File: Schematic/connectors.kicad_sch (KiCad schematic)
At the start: 32 parts, among them J10 PIN2216, J11 PIN2216, J12 PIN2216, J2 PIN2216, J3 PIN2216, J4 PIN2216, J5 PIN2216, J6 PIN2216, J7 PIN2216, J8 PIN2216, J9 PIN2216, U10 HDGC1002WR-S-4P, U11 HDGC1002WR-S-4P, U14 HDGC1002WR-S-4P, U15 HDGC1002WR-S-6P, U16 HDGC1002WR-S-8P, U17 HDGC1002WR-S-8P, U7 HDGC1002WR-S-4P, U8 HDGC1002WR-S-4P, U9 HDGC1002WR-S-4P

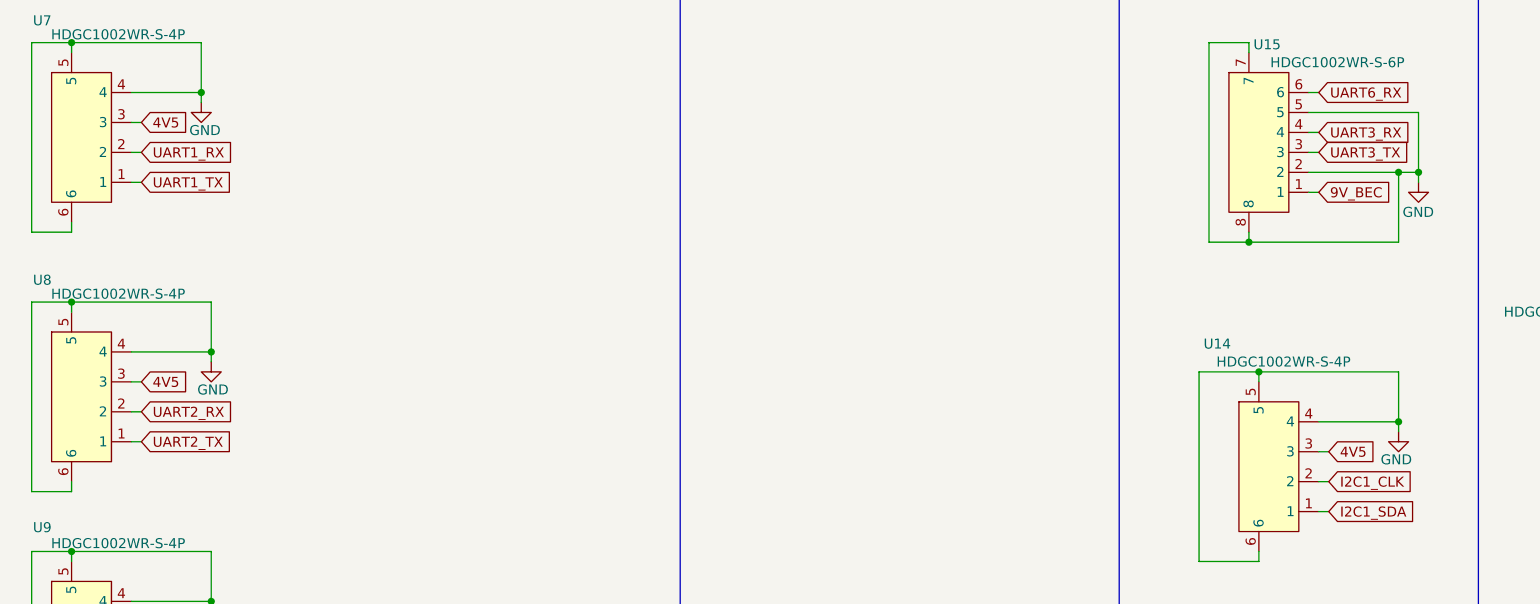
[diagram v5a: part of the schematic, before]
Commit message: Added power zones in Inner2.cu layer for better power management
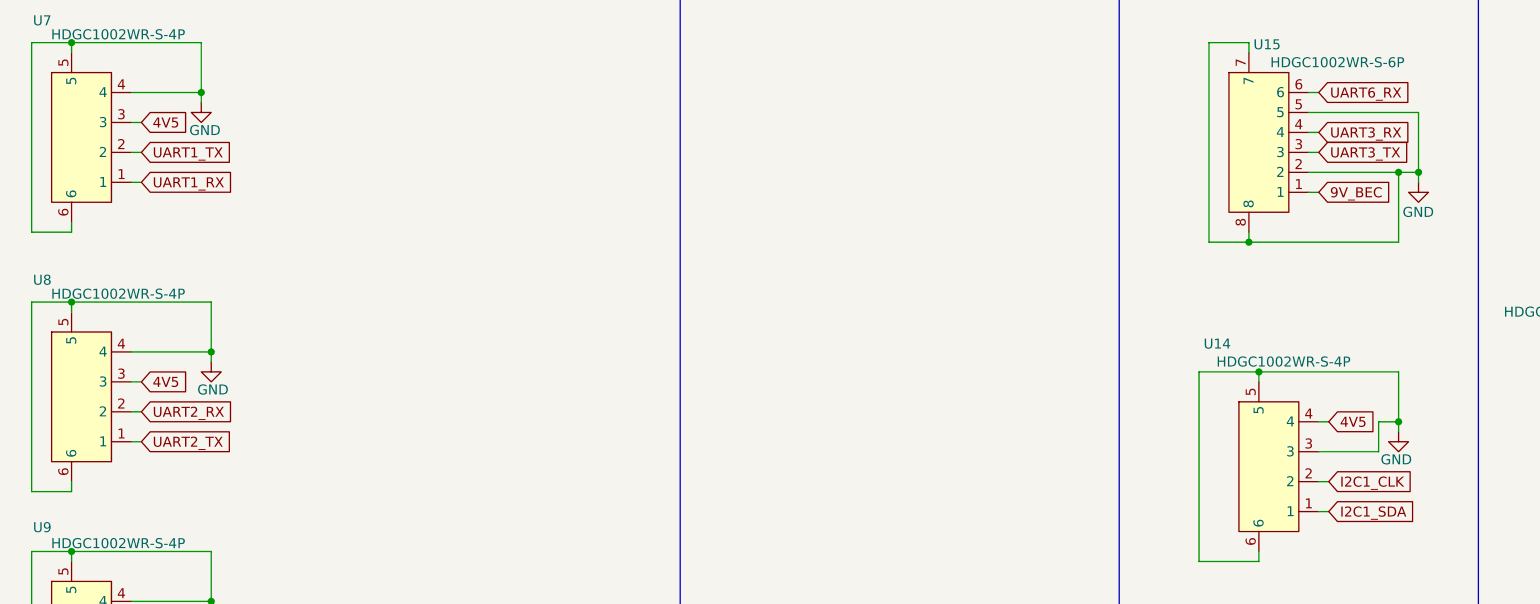
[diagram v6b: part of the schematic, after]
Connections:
- net 4V5: now also U14.4; no longer U14.3
- net GND: now also U14.3; no longer U14.4
- net UART1_RX: now also U7.1; no longer U7.2
- net UART1_TX: now also U7.2; no longer U7.1
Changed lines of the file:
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@@
+	)
+	(junction
+		(at 200.66 45.72)
+		(diameter 0)
+		(color 0 0 0 0)
+	)
+	(junction
+		(at 31.75 62.23)
+		(diameter 0)
+		(color 0 0 0 0)
+	)
+	(junction
+		(at 41.91 144.78)
+		(diameter 0)
+		(color 0 0 0 0)
+	)
+	(junction
+		(at 49.53 68.58)
+		(diameter 0)
+		(color 0 0 0 0)
+	)
+	(junction
+		(at 48.26 35.56)
+		(diameter 0)
+		(color 0 0 0 0)
+	)
+	(junction
+		(at 203.2 45.72)
+		(diameter 0)
+		(color 0 0 0 0)
+	)
+	(junction
+		(at 31.75 185.42)
+		(diameter 0)
+		(color 0 0 0 0)
 	)
 	(junction
@@
 	)
 	(junction
-		(at 200.66 45.72)
-		(diameter 0)
-		(color 0 0 0 0)
-	)
-	(junction
-		(at 31.75 62.23)
-		(diameter 0)
-		(color 0 0 0 0)
-	)
-	(junction
-		(at 41.91 144.78)
-		(diameter 0)
-		(color 0 0 0 0)
-	)
-	(junction
-		(at 49.53 68.58)
-		(diameter 0)
-		(color 0 0 0 0)
-	)
-	(junction
-		(at 48.26 35.56)
-		(diameter 0)
-		(color 0 0 0 0)
-	)
-	(junction
-		(at 203.2 45.72)
-		(diameter 0)
-		(color 0 0 0 0)
-	)
-	(junction
-		(at 31.75 185.42)
-		(diameter 0)
-		(color 0 0 0 0)
-	)
-	(junction
 		(at 181.61 54.61)
 		(diameter 0)
@@
 	(wire
 		(pts
+			(xy 198.12 77.47) (xy 200.66 77.47)
+		)
+		(stroke
+			(width 0)
+			(type default)
+		)
+	)
+	(wire
+		(pts
 			(xy 190.5 85.09) (xy 191.77 85.09)
 		)
@@
 	(wire
 		(pts
-			(xy 200.66 78.74) (xy 200.66 77.47)
+			(xy 200.66 71.12) (xy 200.66 77.47)
 		)
 		(stroke
@@
 	(wire
 		(pts
+			(xy 200.66 77.47) (xy 200.66 78.74)
+		)
+		(stroke
+			(width 0)
+			(type default)
+		)
+	)
+	(wire
+		(pts
 			(xy 247.65 102.87) (xy 250.19 102.87)
 		)
@@
 	(wire
 		(pts
+			(xy 198.12 81.28) (xy 198.12 77.47)
+		)
+		(stroke
+			(width 0)
+			(type default)
+		)
+	)
+	(wire
+		(pts
 			(xy 143.51 106.68) (xy 144.78 106.68)
 		)
@@
 	(wire
 		(pts
-			(xy 190.5 81.28) (xy 191.77 81.28)
-		)
-		(stroke
-			(width 0)
-			(type default)
-		)
-	)
-	(wire
-		(pts
-			(xy 200.66 71.12) (xy 200.66 77.47)
+			(xy 190.5 81.28) (xy 198.12 81.28)
 		)
 		(stroke
@@
 	(wire
 		(pts
+			(xy 190.5 77.47) (xy 191.77 77.47)
+		)
+		(stroke
+			(width 0)
+			(type default)
+		)
+	)
+	(wire
+		(pts
 			(xy 242.57 81.28) (xy 242.57 82.55)
 		)
@@
 		(pts
 			(xy 48.26 29.21) (xy 48.26 35.56)
-		)
-		(stroke
-			(width 0)
-			(type default)
-		)
-	)
-	(wire
-		(pts
-			(xy 190.5 77.47) (xy 200.66 77.47)
 		)
 		(stroke
@@
 	(global_label "4V5"
 		(shape input)
-		(at 191.77 81.28 0)
-		(fields_autoplaced yes)
-		(effects
-			(font
-				(size 1.27 1.27)
-			)
-			(justify left)
-		)
-		(property "Intersheetrefs" "${INTERSHEET_REFS}"
-			(at 198.2628 81.28 0)
+		(at 191.77 77.47 0)
+		(fields_autoplaced yes)
+		(effects
+			(font
+				(size 1.27 1.27)
+			)
+			(justify left)
+		)
+		(property "Intersheetrefs" "${INTERSHEET_REFS}"
+			(at 198.2628 77.47 0)
 			(effects
 				(font
@@
 	(global_label "UART1_TX"
 		(shape input)
+		(at 40.64 43.18 0)
+		(fields_autoplaced yes)
+		(effects
+			(font
+				(size 1.27 1.27)
+			)
+			(justify left)
+		)
+		(property "Intersheetrefs" "${INTERSHEET_REFS}"
+			(at 52.6361 43.18 0)
+			(effects
+				(font
+					(size 1.27 1.27)
+				)
+				(justify left)
+				(hide yes)
+			)
+		)
+	)
+	(global_label "UART1_RX"
+		(shape input)
 		(at 40.64 46.99 0)
 		(fields_autoplaced yes)
@@
 		)
 		(property "Intersheetrefs" "${INTERSHEET_REFS}"
-			(at 52.6361 46.99 0)
-			(effects
-				(font
-					(size 1.27 1.27)
-				)
-				(justify left)
-				(hide yes)
-			)
-		)
-	)
-	(global_label "UART1_RX"
-		(shape input)
-		(at 40.64 43.18 0)
-		(fields_autoplaced yes)
-		(effects
-			(font
-				(size 1.27 1.27)
-			)
-			(justify left)
-		)
-		(property "Intersheetrefs" "${INTERSHEET_REFS}"
-			(at 52.9385 43.18 0)
-			(effects
-				(font
+			(at 52.9385 46.99 0)
+			(effects
+				(font

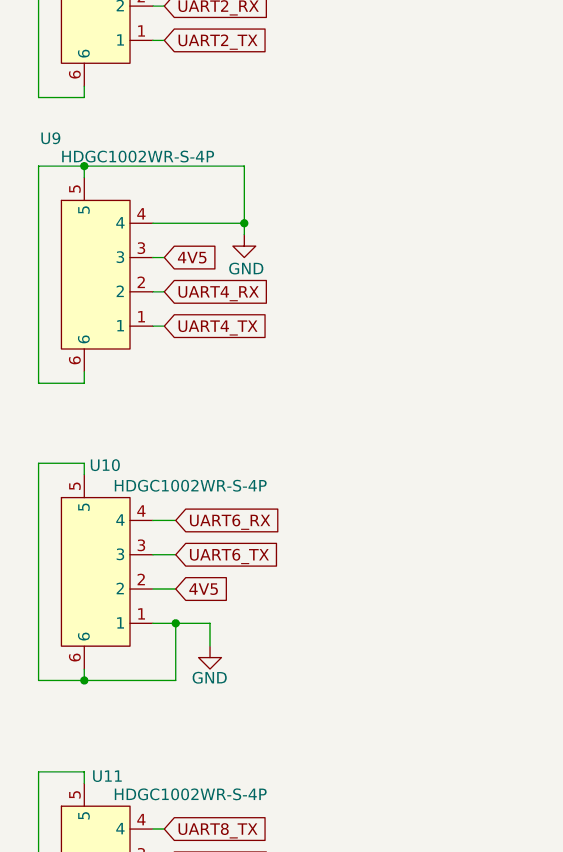
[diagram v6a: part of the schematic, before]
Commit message: still routing and defining plan zones for power nets
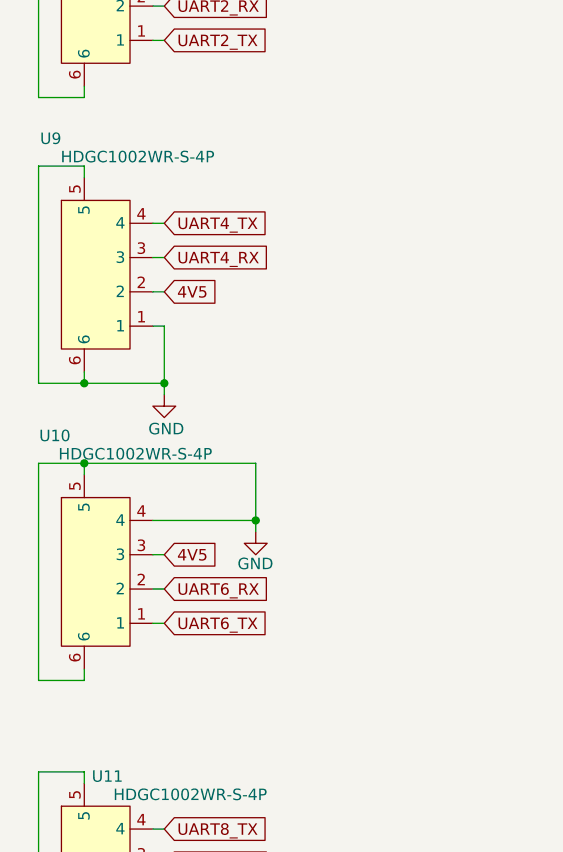
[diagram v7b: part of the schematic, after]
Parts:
- TP1, TP2, TP3, TP4, TP5, TP6, TP7: footprint TestPoint:TestPoint_Pad_1.0x1.0mm -> fch7_fp:TestPoint_Pad_D0.8
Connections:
- net 4V5: now also U10.3, U9.2; no longer U10.2, U9.3
- net GND: now also U10.4, U9.1; no longer U10.1, U9.4
- net UART4_RX: now also U9.3; no longer U9.2
- net UART4_TX: now also U9.4; no longer U9.1
- net UART6_RX: now also U10.2; no longer U10.4
- net UART6_TX: now also U10.1; no longer U10.3

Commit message: Still routing...
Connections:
- net PWM1: now also RN2.1, U17.8; no longer RN2.4, U17.5
- net PWM2: now also RN2.2, U17.7; no longer RN2.3, U17.6
- net PWM3: now also RN2.3, U17.6; no longer RN2.2, U17.7
- net PWM4: now also RN2.4, U17.5; no longer RN2.1, U17.8
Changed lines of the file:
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@@
 	)
 	(label "PWM1"
-		(at 250.19 95.25 0)
+		(at 250.19 87.63 0)
 		(effects
 			(font
@@
 	)
 	(label "PWM4"
-		(at 250.19 87.63 0)
+		(at 250.19 95.25 0)
 		(effects
 			(font
@@
 	)
 	(label "PWM3"
-		(at 250.19 90.17 0)
+		(at 250.19 92.71 0)
 		(effects
 			(font
@@
 	)
 	(label "PWM2"
-		(at 250.19 92.71 0)
+		(at 250.19 90.17 0)
 		(effects
 			(font
